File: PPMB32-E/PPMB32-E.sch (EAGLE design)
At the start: 36 parts, among them IC1 7805TV, IC2 LM3940IT-3.3, K1 ARK500/2, K2 ARK500/2, K3 ARK500/2, K4 ARK500/2, K5 ARK500/2

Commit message: First development version of PPMB32-E
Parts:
- removed K6: (no value), #PaJa_konektory:PSH02-03P
- added DHT0, DHT1, DHT2, DHT3, GPIO16, GPIO23, GPIO26: (no value), pinhead:PINHD-1X3
- added OW_DATA: (no value), pinhead:PINHD-1X10
- added OW_PWR: (no value), pinhead:PINHD-2X10
- added SJ1: (no value), jumper:SJ
- added SVC: (no value), pinhead:PINHD-2X4
- JP3: device pinhead:PINHD-2X4 -> jumper:JP2E
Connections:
- new net +5V: DHT0.2, DHT1.2, DHT2.2, DHT3.2, GPIO16.2, GPIO23.2, GPIO26.2, JP3.3, SJ1.2
- new net N$11: JP3.2, OW_PWR.1, OW_PWR.11, OW_PWR.13, OW_PWR.15, OW_PWR.17, OW_PWR.19, OW_PWR.3, OW_PWR.5, OW_PWR.7, OW_PWR.9, SJ1.1
- net +3V3: now also JP3.1
- net ESP_EN: now also SVC.1; no longer JP3.1
- net GND: now also DHT0.1, DHT1.1, DHT2.1, DHT3.1, GPIO16.1, GPIO23.1, GPIO26.1, OW_PWR.10, OW_PWR.12, OW_PWR.14, OW_PWR.16, OW_PWR.18, OW_PWR.2, OW_PWR.20, OW_PWR.4, OW_PWR.6, OW_PWR.8, SVC.3, SVC.5, SVC.7
- net GPIO16: now also GPIO16.3
- net GPIO17: now also DHT3.3
- net GPIO18: now also DHT1.3
- net GPIO19: now also DHT0.3
- net GPIO23: now also GPIO23.3; no longer JP3.5
- net GPIO26: now also GPIO26.3; no longer JP3.3
- net GPIO5: now also DHT2.3; no longer JP3.7
- net ONE_WIRE: now also OW_DATA.1, OW_DATA.10, OW_DATA.2, OW_DATA.3, OW_DATA.4, OW_DATA.5, OW_DATA.6, OW_DATA.7, OW_DATA.8, OW_DATA.9
- net SVN: now also SVC.4; no longer JP3.4
- net SVP: now also SVC.2; no longer JP3.2
- net UART0_RXD: now also SVC.8; no longer JP3.8
- net UART0_TXD: now also SVC.6; no longer JP3.6

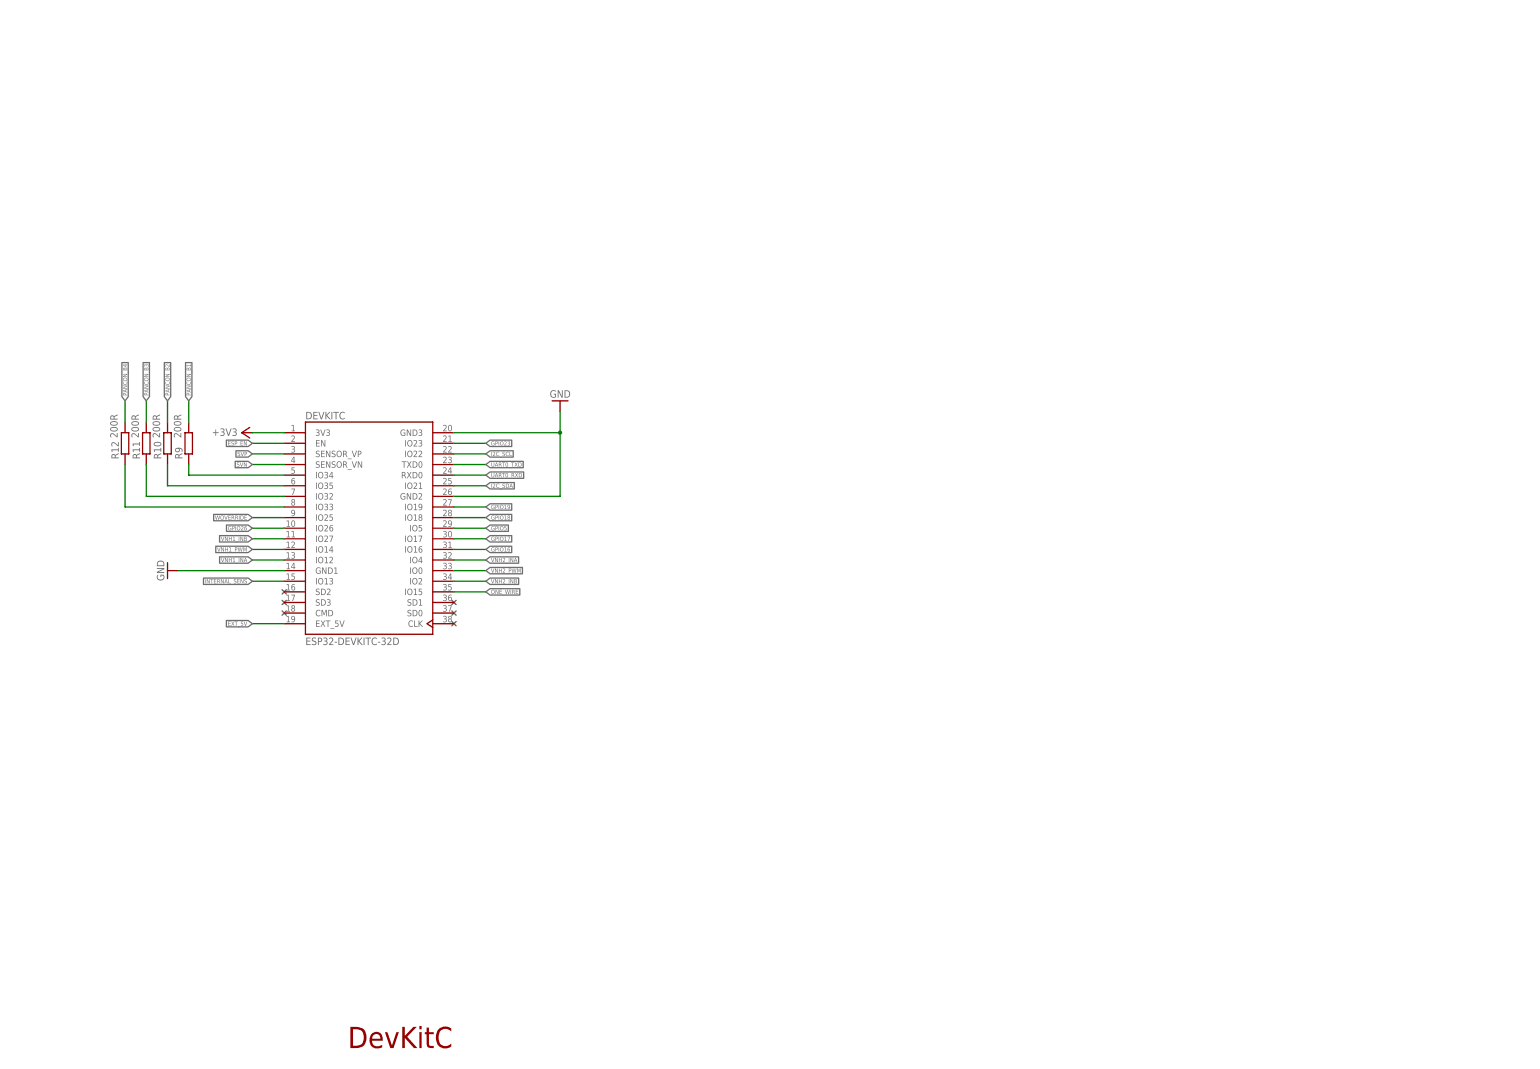
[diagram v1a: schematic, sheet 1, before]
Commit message: Remove obsolete files, pre-release versions of PPSB-T & PPSB-TH
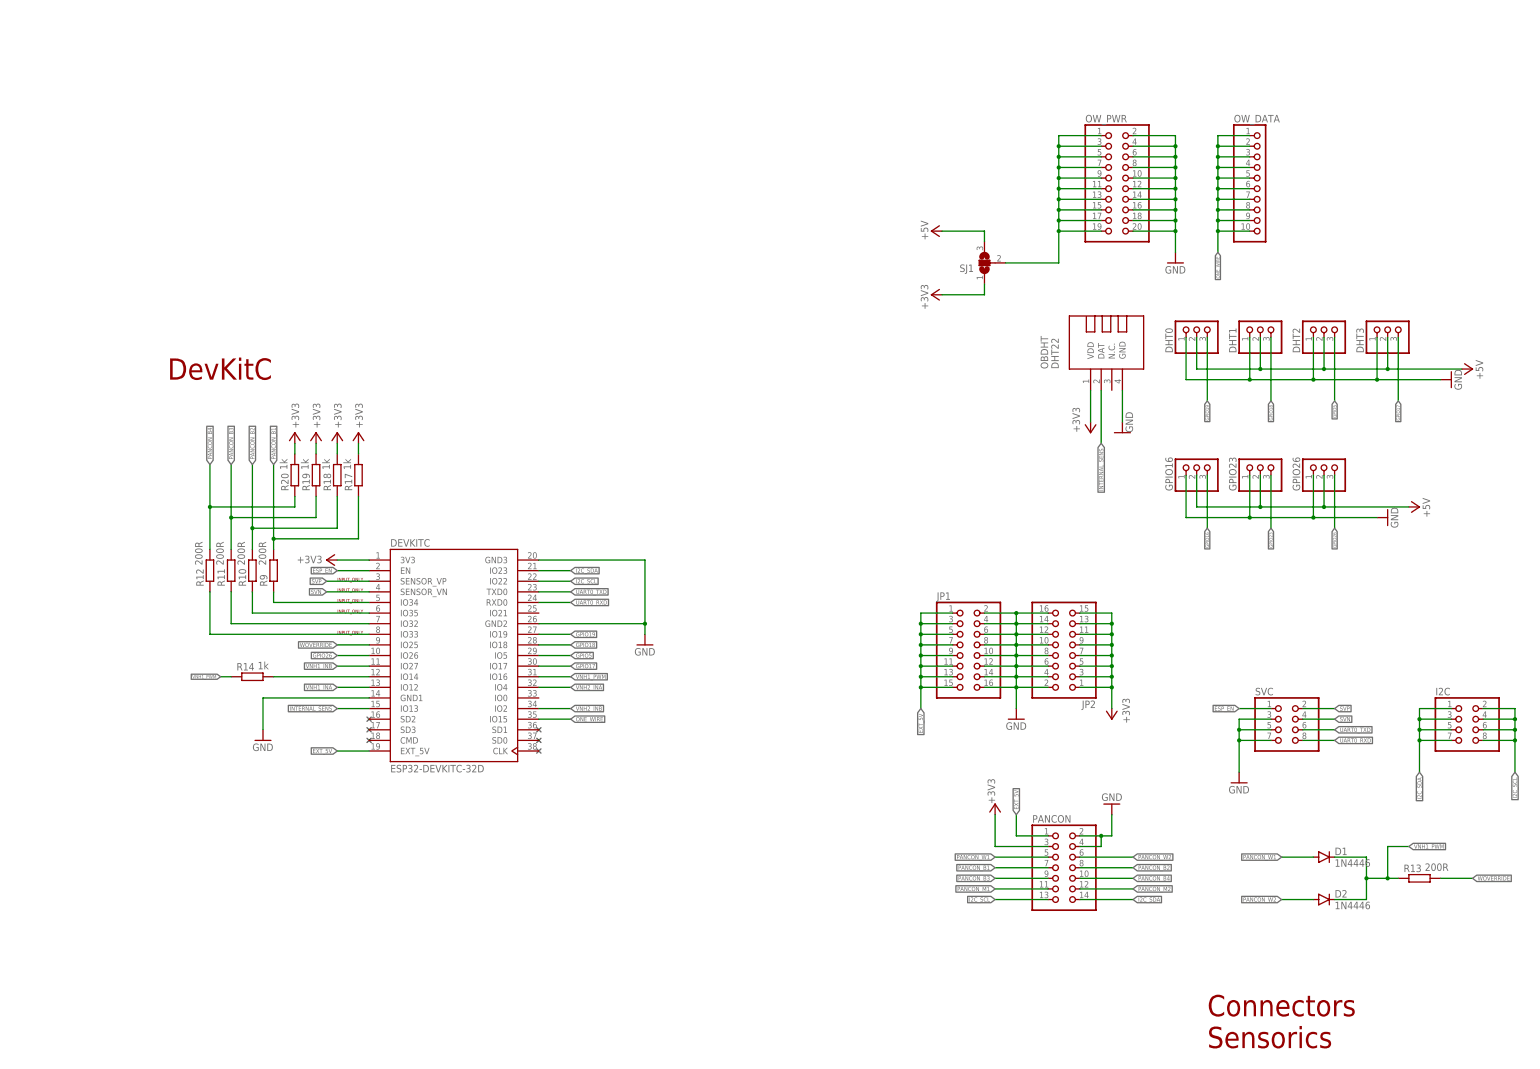
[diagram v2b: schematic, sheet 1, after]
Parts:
- removed JP3: (no value), jumper:JP2E
- added R14, R15, R16, R17, R18, R19, R20: 1k, rcl:R-EU_R0603
- SJ1: device jumper:SJ -> jumper:SJ2W
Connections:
- new net N$12: DEVKITC.IO14, R14.2
- net +3V3: now also R17.2, R18.2, R19.2, R20.2, SJ1.1; no longer JP3.1
- net +5V: now also SJ1.3; no longer JP3.3, SJ1.2
- net GND: now also R15.1, R16.1
- net GPIO16: no longer DEVKITC.IO16
- net GPIO23: no longer DEVKITC.IO23
- net I2C_SDA: now also DEVKITC.IO23; no longer DEVKITC.IO21
- net N$11: now also SJ1.2; no longer JP3.2, SJ1.1
- net PANCON_B1: now also R17.1
- net PANCON_B2: now also R18.1
- net PANCON_B3: now also R19.1
- net PANCON_B4: now also R20.1
- net VNH1_INA: now also R16.2
- net VNH1_INB: now also R15.2
- net VNH1_PWM: now also DEVKITC.IO16, R14.1; no longer DEVKITC.IO14
- net VNH2_PWM: no longer DEVKITC.IO0
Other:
- note added: "INPUT_ONLY"
- moved on the sheet: DEVKITC, K1, K2, K3, R10, R11, R12, R4, R9

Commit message: Improved schematics layout.
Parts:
- added SJ2, SJ3: (no value), jumper:SJ
- D1, D2: value 1N4446 -> BAT85; device diode:1N4446 -> adafruit:SCHOTTKY-DIODEDO35-7
- R10, R11, R12, R9: value 200R -> 270R
- R15, R16, R4, R8: value 1k -> 47k
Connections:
- net PANCON_W1: now also SJ3.2
- net PANCON_W2: now also SJ2.2
- net VNH1_INA: now also SJ3.1
- net VNH1_INB: now also SJ2.1
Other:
- note added: "Created by Petr Stourac, sourced under CC BY-NC-SA v3.0 licence Distributed "AS IS" without warranty of any kind, espress or implied, including but not limited to the warranties of merchantability or noninfringement."
- note added: "DevKit Connectors"
- note added: "PROTOPlant system motherboard"
- note added: "PWROUT Power"
- note added: "ver. 1 rev. 0"
- note removed: "Connectors Sensorics"
- note removed: "DevKitC"
- note removed: "Power"
